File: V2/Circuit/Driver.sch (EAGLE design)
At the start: 32 parts, among them IC1 DRV8300DIPWR, IC2 CD74HC4049PWR, U1 INA240A1PWR, U2 INA240A1PWR, U3 INA240A1PWR

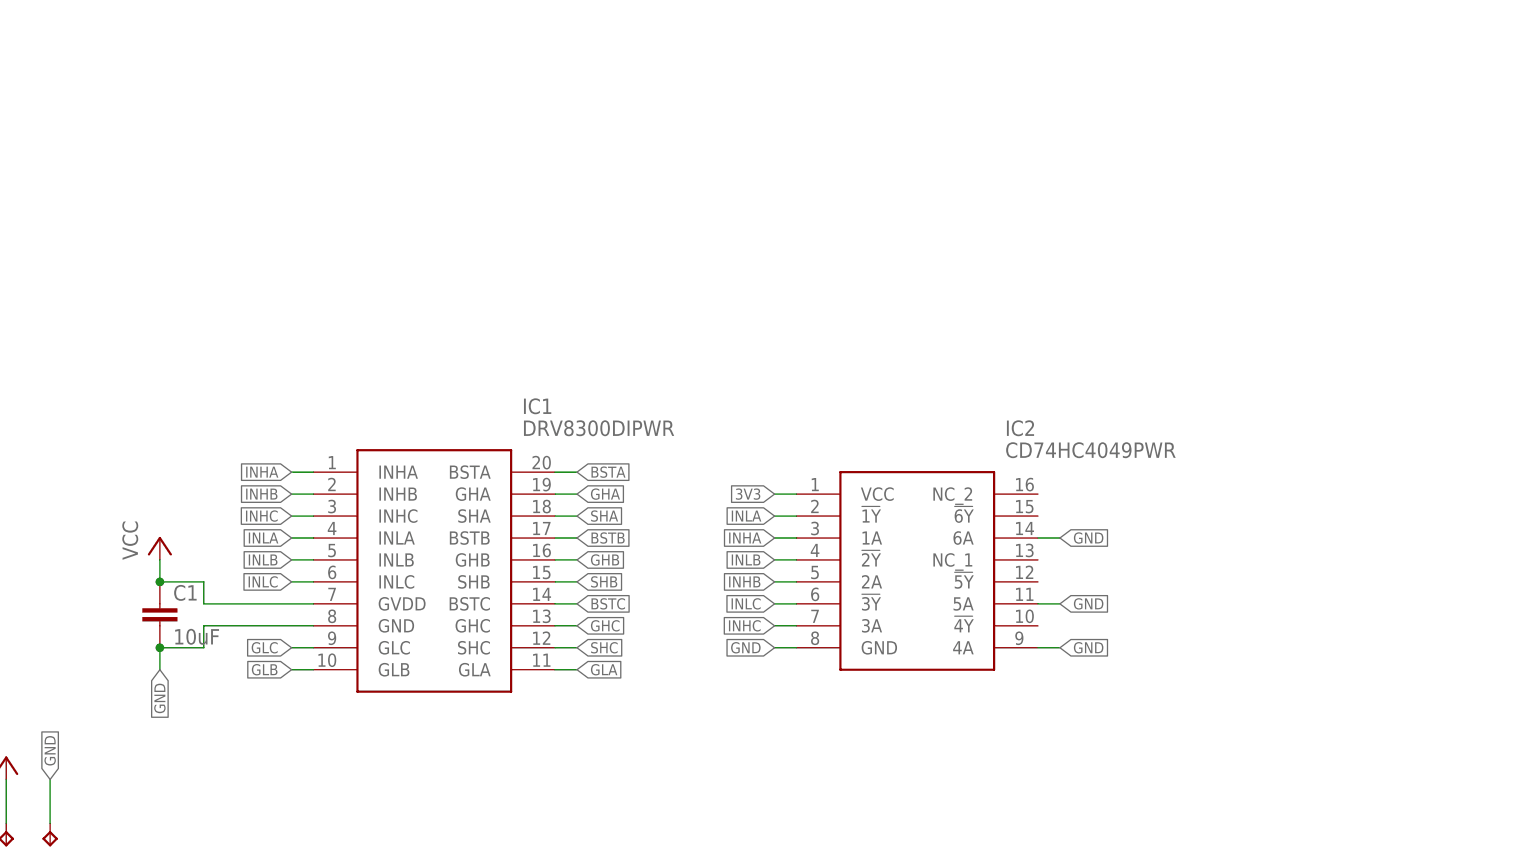
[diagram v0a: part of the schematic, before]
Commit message: Designed V2, Ready for autoroutering 1
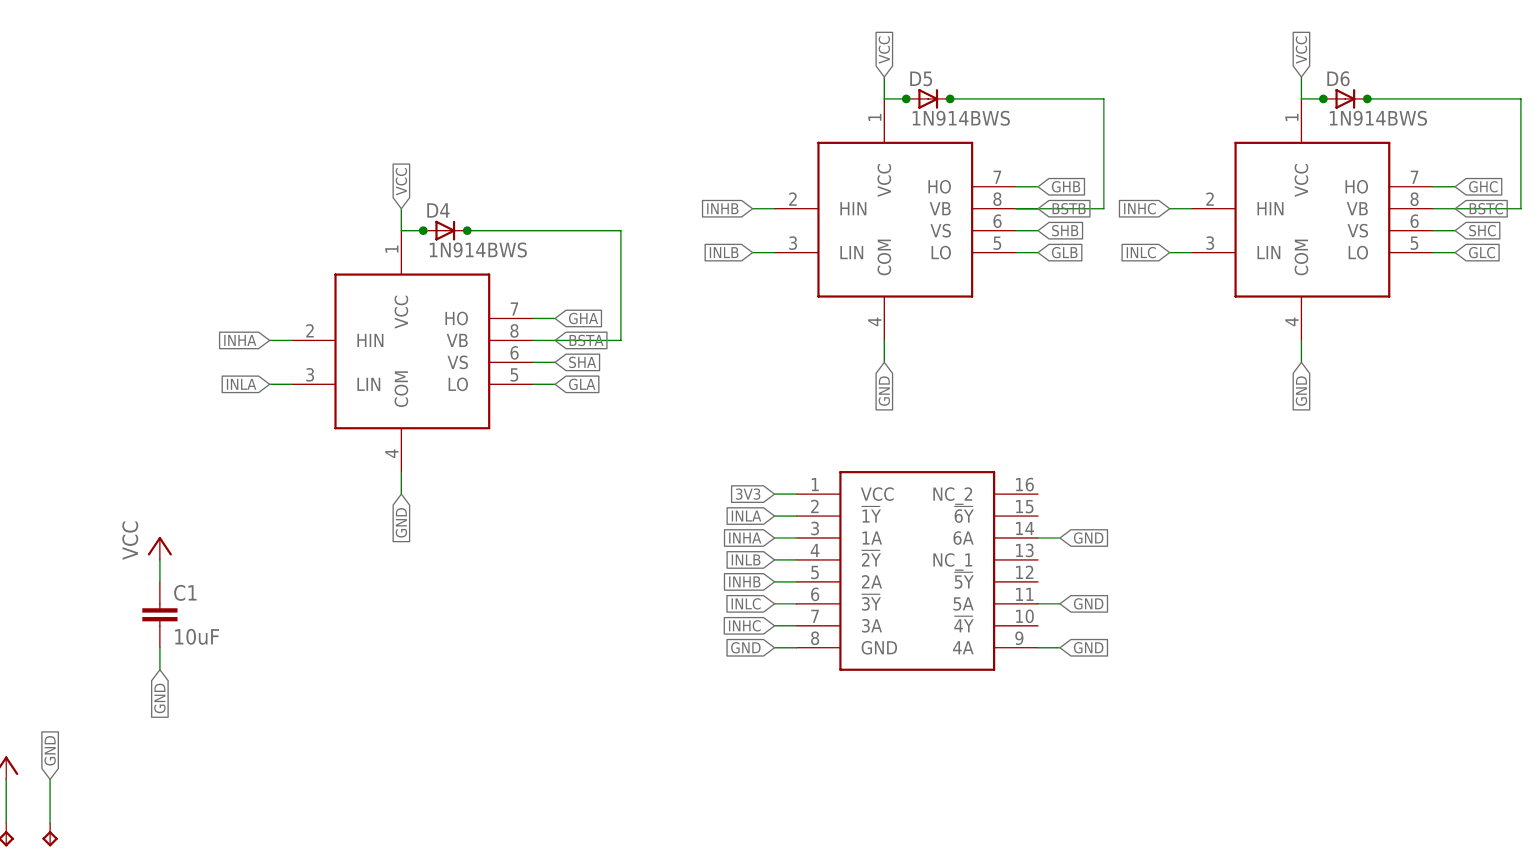
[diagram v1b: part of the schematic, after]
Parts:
- removed IC1: DRV8300DIPWR, DRV8300DIPWR:DRV8300DIPWR
- added D4, D5, D6: 1N914BWS, _hhn_diodes_smd:1N914BWS
- added U4, U5, U6: SOIC127P610X320-8NSOIC8, SOIC127P610X320-8N:SOIC127P610X320-8NSOIC8
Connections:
- net BSTA: now also D4.C, U4.VB; no longer IC1.BSTA
- net BSTB: now also D5.C, U5.VB; no longer IC1.BSTB
- net BSTC: now also D6.C, U6.VB; no longer IC1.BSTC
- net GHA: now also U4.HO; no longer IC1.GHA
- net GHB: now also U5.HO; no longer IC1.GHB
- net GHC: now also U6.HO; no longer IC1.GHC
- net GLA: now also U4.LO; no longer IC1.GLA
- net GLB: now also U5.LO; no longer IC1.GLB
- net GLC: now also U6.LO; no longer IC1.GLC
- net GND: now also U4.COM, U5.COM, U6.COM; no longer IC1.GND
- net INHA: now also U4.HIN; no longer IC1.INHA
- net INHB: now also U5.HIN; no longer IC1.INHB
- net INHC: now also U6.HIN; no longer IC1.INHC
- net INLA: now also U4.LIN; no longer IC1.INLA
- net INLB: now also U5.LIN; no longer IC1.INLB
- net INLC: now also U6.LIN; no longer IC1.INLC
- net SHA: now also U4.VS; no longer IC1.SHA
- net SHB: now also U5.VS; no longer IC1.SHB
- net SHC: now also U6.VS; no longer IC1.SHC
- net VCC: now also D4.A, D5.A, D6.A, U4.VCC, U5.VCC, U6.VCC; no longer IC1.GVDD

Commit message: Generated the Gerber files of the circuit
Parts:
- renumbered U$2 to H-A, U$3 to L-A, U$4 to H-B, U$5 to L-B, U$6 to H-C, U$7 to L-C
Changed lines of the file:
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@@
 <part name="P+1" library="supply1" library_urn="urn:adsk.eagle:library:371" deviceset="VCC" device=""/>
 <part name="P+2" library="supply1" library_urn="urn:adsk.eagle:library:371" deviceset="VCC" device=""/>
-<part name="U$2" library="BLDC project" deviceset="IRLR7843" device=""/>
-<part name="U$3" library="BLDC project" deviceset="IRLR7843" device=""/>
-<part name="U$6" library="BLDC project" deviceset="IRLR7843" device=""/>
-<part name="U$7" library="BLDC project" deviceset="IRLR7843" device=""/>
+<part name="H-A" library="BLDC project" deviceset="IRLR7843" device=""/>
+<part name="L-A" library="BLDC project" deviceset="IRLR7843" device=""/>
+<part name="H-C" library="BLDC project" deviceset="IRLR7843" device=""/>
+<part name="L-C" library="BLDC project" deviceset="IRLR7843" device=""/>
 <part name="P+3" library="supply1" library_urn="urn:adsk.eagle:library:371" deviceset="VCC" device=""/>
 <part name="P+5" library="supply1" library_urn="urn:adsk.eagle:library:371" deviceset="VCC" device=""/>
@@
 <part name="R5" library="SparkFun-Resistors" deviceset="100OHM" device="-0603-1/10W-1%" value="100"/>
 <part name="R6" library="SparkFun-Resistors" deviceset="100OHM" device="-0603-1/10W-1%" value="100"/>
-<part name="U$4" library="BLDC project" deviceset="IRLR7843" device=""/>
-<part name="U$5" library="BLDC project" deviceset="IRLR7843" device=""/>
+<part name="H-B" library="BLDC project" deviceset="IRLR7843" device=""/>
+<part name="L-B" library="BLDC project" deviceset="IRLR7843" device=""/>
 <part name="P+4" library="supply1" library_urn="urn:adsk.eagle:library:371" deviceset="VCC" device=""/>
 <part name="C2" library="SparkFun-Capacitors" deviceset="1.0UF" device="-0603-16V-10%" value="1.0uF"/>
@@
 <attribute name="VALUE" x="134.62" y="109.22" size="1.778" layer="96" rot="R90"/>
 </instance>
-<instance part="U$2" gate="G$1" x="157.48" y="60.96" smashed="yes"/>
-<instance part="U$3" gate="G$1" x="157.48" y="43.18" smashed="yes"/>
-<instance part="U$6" gate="G$1" x="208.28" y="60.96" smashed="yes"/>
-<instance part="U$7" gate="G$1" x="208.28" y="43.18" smashed="yes"/>
+<instance part="H-A" gate="G$1" x="157.48" y="60.96" smashed="yes"/>
+<instance part="L-A" gate="G$1" x="157.48" y="43.18" smashed="yes"/>
+<instance part="H-C" gate="G$1" x="208.28" y="60.96" smashed="yes"/>
+<instance part="L-C" gate="G$1" x="208.28" y="43.18" smashed="yes"/>
 <instance part="P+3" gate="VCC" x="160.02" y="73.66" smashed="yes">
 <attribute name="VALUE" x="157.48" y="71.12" size="1.778" layer="96" rot="R90"/>
@@
 <attribute name="VALUE" x="172.72" y="39.116" size="1.778" layer="96" font="vector" align="top-center"/>
 </instance>
-<instance part="U$4" gate="G$1" x="182.88" y="60.96" smashed="yes"/>
-<instance part="U$5" gate="G$1" x="182.88" y="43.18" smashed="yes"/>
+<instance part="H-B" gate="G$1" x="182.88" y="60.96" smashed="yes"/>
+<instance part="L-B" gate="G$1" x="182.88" y="43.18" smashed="yes"/>
 <instance part="P+4" gate="VCC" x="185.42" y="73.66" smashed="yes">
 <attribute name="VALUE" x="182.88" y="71.12" size="1.778" layer="96" rot="R90"/>
@@
 </segment>
 <segment>
-<pinref part="U$3" gate="G$1" pin="S"/>
+<pinref part="L-A" gate="G$1" pin="S"/>
 <wire x1="160.02" y1="38.1" x2="160.02" y2="30.48" width="0.1524" layer="91"/>
 <label x="160.02" y="30.48" size="1.27" layer="95" rot="R270" xref="yes"/>
 </segment>
 <segment>
-<pinref part="U$7" gate="G$1" pin="S"/>
+<pinref part="L-C" gate="G$1" pin="S"/>
 <wire x1="210.82" y1="38.1" x2="210.82" y2="30.48" width="0.1524" layer="91"/>
 <label x="210.82" y="30.48" size="1.27" layer="95" rot="R270" xref="yes"/>
 </segment>
 <segment>
-<pinref part="U$5" gate="G$1" pin="S"/>
+<pinref part="L-B" gate="G$1" pin="S"/>
 <wire x1="185.42" y1="38.1" x2="185.42" y2="30.48" width="0.1524" layer="91"/>
 <label x="185.42" y="30.48" size="1.27" layer="95" rot="R270" xref="yes"/>
@@
 <pinref part="D4" gate="G$1" pin="C"/>
 <junction x="172.72" y="147.32"/>
+<junction x="180.34" y="134.62"/>
 </segment>
 </net>
@@
 <net name="SHA" class="0">
 <segment>
-<pinref part="U$2" gate="G$1" pin="S"/>
+<pinref part="H-A" gate="G$1" pin="S"/>
 <wire x1="160.02" y1="55.88" x2="160.02" y2="53.34" width="0.1524" layer="91"/>
-<pinref part="U$3" gate="G$1" pin="D"/>
+<pinref part="L-A" gate="G$1" pin="D"/>
 <wire x1="160.02" y1="53.34" x2="160.02" y2="48.26" width="0.1524" layer="91"/>
 <wire x1="160.02" y1="53.34" x2="162.56" y2="53.34" width="0.1524" layer="91"/>
@@
 <pinref part="D5" gate="G$1" pin="C"/>
 <junction x="228.6" y="162.56"/>
+<junction x="236.22" y="149.86"/>
 </segment>
 </net>
@@
 <net name="SHB" class="0">
 <segment>
-<pinref part="U$4" gate="G$1" pin="S"/>
+<pinref part="H-B" gate="G$1" pin="S"/>
 <wire x1="185.42" y1="55.88" x2="185.42" y2="53.34" width="0.1524" layer="91"/>
-<pinref part="U$5" gate="G$1" pin="D"/>
+<pinref part="L-B" gate="G$1" pin="D"/>
 <wire x1="185.42" y1="53.34" x2="185.42" y2="48.26" width="0.1524" layer="91"/>
 <wire x1="185.42" y1="48.26" x2="185.42" y2="45.72" width="0.1524" layer="91"/>
@@
 <pinref part="D6" gate="G$1" pin="C"/>
 <junction x="276.86" y="162.56"/>
+<junction x="284.48" y="149.86"/>
 </segment>
 </net>
@@
 <net name="SHC" class="0">
 <segment>
-<pinref part="U$6" gate="G$1" pin="S"/>
+<pinref part="H-C" gate="G$1" pin="S"/>
 <wire x1="210.82" y1="55.88" x2="210.82" y2="53.34" width="0.1524" layer="91"/>
-<pinref part="U$7" gate="G$1" pin="D"/>
+<pinref part="L-C" gate="G$1" pin="D"/>
 <wire x1="210.82" y1="53.34" x2="210.82" y2="48.26" width="0.1524" layer="91"/>
 <wire x1="210.82" y1="48.26" x2="210.82" y2="45.72" width="0.1524" layer="91"/>
@@
 <segment>
 <pinref part="P+3" gate="VCC" pin="VCC"/>
-<pinref part="U$2" gate="G$1" pin="D"/>
+<pinref part="H-A" gate="G$1" pin="D"/>
 <wire x1="160.02" y1="71.12" x2="160.02" y2="66.04" width="0.1524" layer="91"/>
 </segment>
 <segment>
 <pinref part="P+5" gate="VCC" pin="VCC"/>
-<pinref part="U$6" gate="G$1" pin="D"/>
+<pinref part="H-C" gate="G$1" pin="D"/>
 <wire x1="210.82" y1="71.12" x2="210.82" y2="66.04" width="0.1524" layer="91"/>
 </segment>
 <segment>
 <pinref part="P+4" gate="VCC" pin="VCC"/>
-<pinref part="U$4" gate="G$1" pin="D"/>
+<pinref part="H-B" gate="G$1" pin="D"/>
 <wire x1="185.42" y1="71.12" x2="185.42" y2="66.04" width="0.1524" layer="91"/>
 </segment>
@@
 <pinref part="D4" gate="G$1" pin="A"/>
 <junction x="167.64" y="147.32"/>
+<junction x="165.1" y="147.32"/>
 </segment>
 <segment>
@@
 <pinref part="D5" gate="G$1" pin="A"/>
 <junction x="223.52" y="162.56"/>
+<junction x="220.98" y="162.56"/>
 </segment>
 <segment>
@@
 <pinref part="D6" gate="G$1" pin="A"/>
 <junction x="271.78" y="162.56"/>
+<junction x="269.24" y="162.56"/>
 </segment>
 </net>
 <net name="N$1" class="0">
 <segment>
-<pinref part="U$2" gate="G$1" pin="G"/>
+<pinref part="H-A" gate="G$1" pin="G"/>
 <wire x1="154.94" y1="58.42" x2="152.4" y2="58.42" width="0.1524" layer="91"/>
 <pinref part="R1" gate="G$1" pin="2"/>
@@
 <net name="N$3" class="0">
 <segment>
-<pinref part="U$6" gate="G$1" pin="G"/>
+<pinref part="H-C" gate="G$1" pin="G"/>
 <wire x1="205.74" y1="58.42" x2="203.2" y2="58.42" width="0.1524" layer="91"/>
 <pinref part="R3" gate="G$1" pin="2"/>
@@
 <net name="N$4" class="0">
 <segment>
-<pinref part="U$3" gate="G$1" pin="G"/>
+<pinref part="L-A" gate="G$1" pin="G"/>
 <wire x1="154.94" y1="40.64" x2="152.4" y2="40.64" width="0.1524" layer="91"/>
 <pinref part="R5" gate="G$1" pin="2"/>
@@
 <net name="N$6" class="0">
 <segment>
-<pinref part="U$7" gate="G$1" pin="G"/>
+<pinref part="L-C" gate="G$1" pin="G"/>
 <wire x1="205.74" y1="40.64" x2="203.2" y2="40.64" width="0.1524" layer="91"/>
 <pinref part="R4" gate="G$1" pin="2"/>
@@
 <net name="N$2" class="0">
 <segment>
-<pinref part="U$4" gate="G$1" pin="G"/>
+<pinref part="H-B" gate="G$1" pin="G"/>
 <wire x1="180.34" y1="58.42" x2="177.8" y2="58.42" width="0.1524" layer="91"/>
 <pinref part="R2" gate="G$1" pin="2"/>
@@
 <net name="N$5" class="0">
 <segment>
-<pinref part="U$5" gate="G$1" pin="G"/>
+<pinref part="L-B" gate="G$1" pin="G"/>
 <wire x1="180.34" y1="40.64" x2="177.8" y2="40.64" width="0.1524" layer="91"/>
 <pinref part="R6" gate="G$1" pin="2"/>
